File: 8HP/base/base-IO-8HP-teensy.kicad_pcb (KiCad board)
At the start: 2 copper layers, 39.3 x 100 mm, 13 parts, among them J1 IN, J2 OUT, J3 EURO_POWER_2x6, U1 Teensy3.6

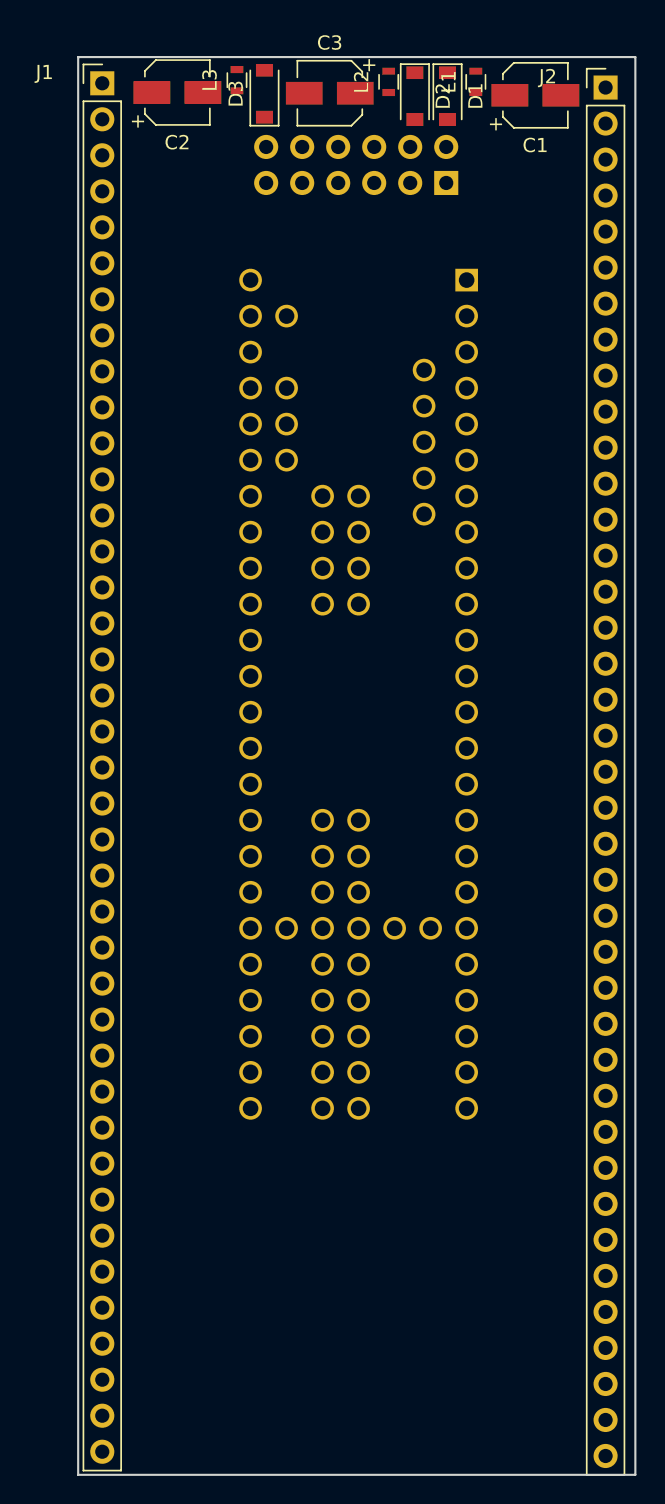
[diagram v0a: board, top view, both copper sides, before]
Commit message: Add a simplified Teensy 3.6 symbol and footprint
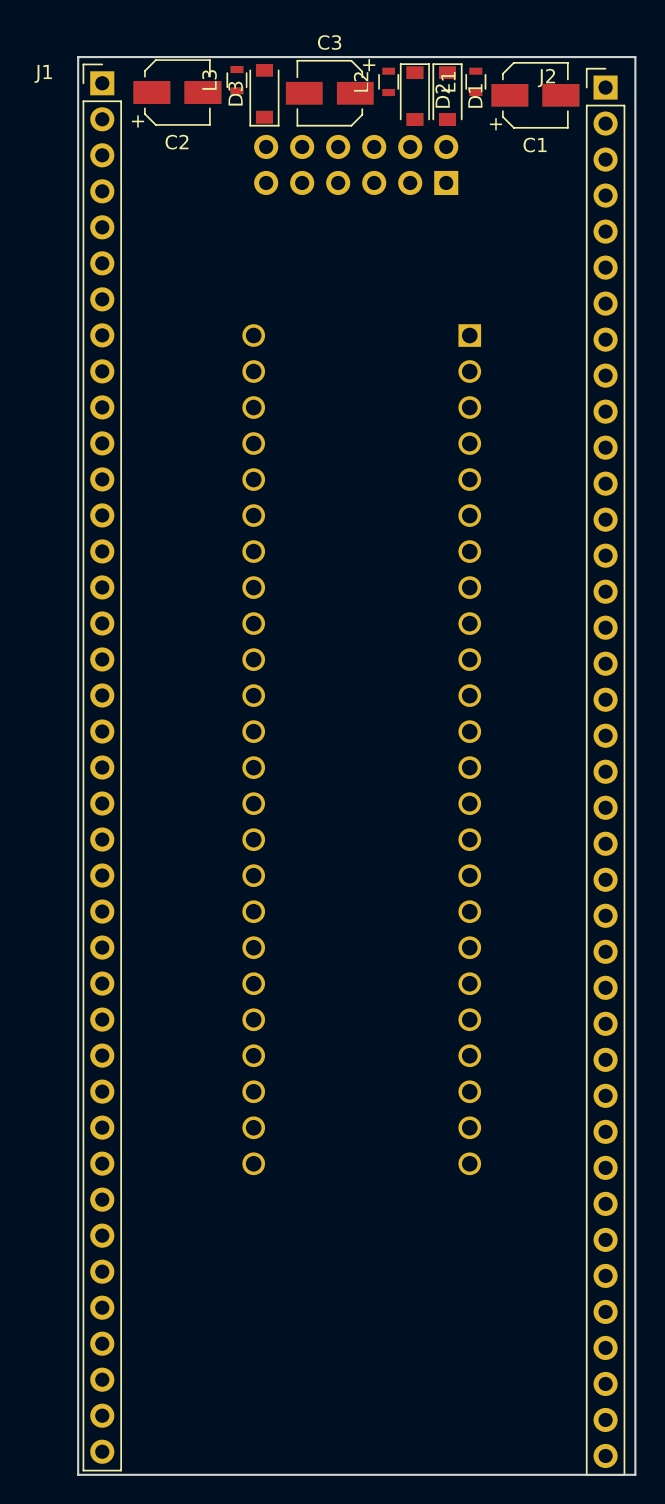
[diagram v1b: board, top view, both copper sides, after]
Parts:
- U1: value Teensy3.6 -> Teensy3.6_Lite; footprint krachmacher:Teensy35_36 -> krachmacher:Teensy35_36_Lite
- moved U1 3.92 mm to (135.5, 87.1)
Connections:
- J1 pad 4: Net-(J1-Pad4) -> +3V3
- J2 pad 4: Net-(J2-Pad4) -> +3V3
- U1 pad 1: Net-(U1-Pad1) -> GND
- U1 pad 15: Net-(U1-Pad15) -> +3V3
- U1 pad 39: Net-(U1-Pad39) -> GND
- U1 pad 51: Net-(U1-Pad51) -> +3V3
- U1 pad 52: Net-(U1-Pad52) -> GND
